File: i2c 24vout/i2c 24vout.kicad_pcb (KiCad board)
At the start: 2 copper layers, 131.2 x 55 mm, 79 parts, among them J1 power in, J2 Conn_01x04, J3 Conn_01x04, J4 Conn_01x04, J5 Conn_01x04, J6 to qwiic breakout, J8 Conn_01x01, J9 Conn_01x01, U1 ILQ620GB-X009, U2 ILQ620GB-X009, U3 ILQ620GB-X009, U4 ILQ620GB-X009, U5 PCA9685PW

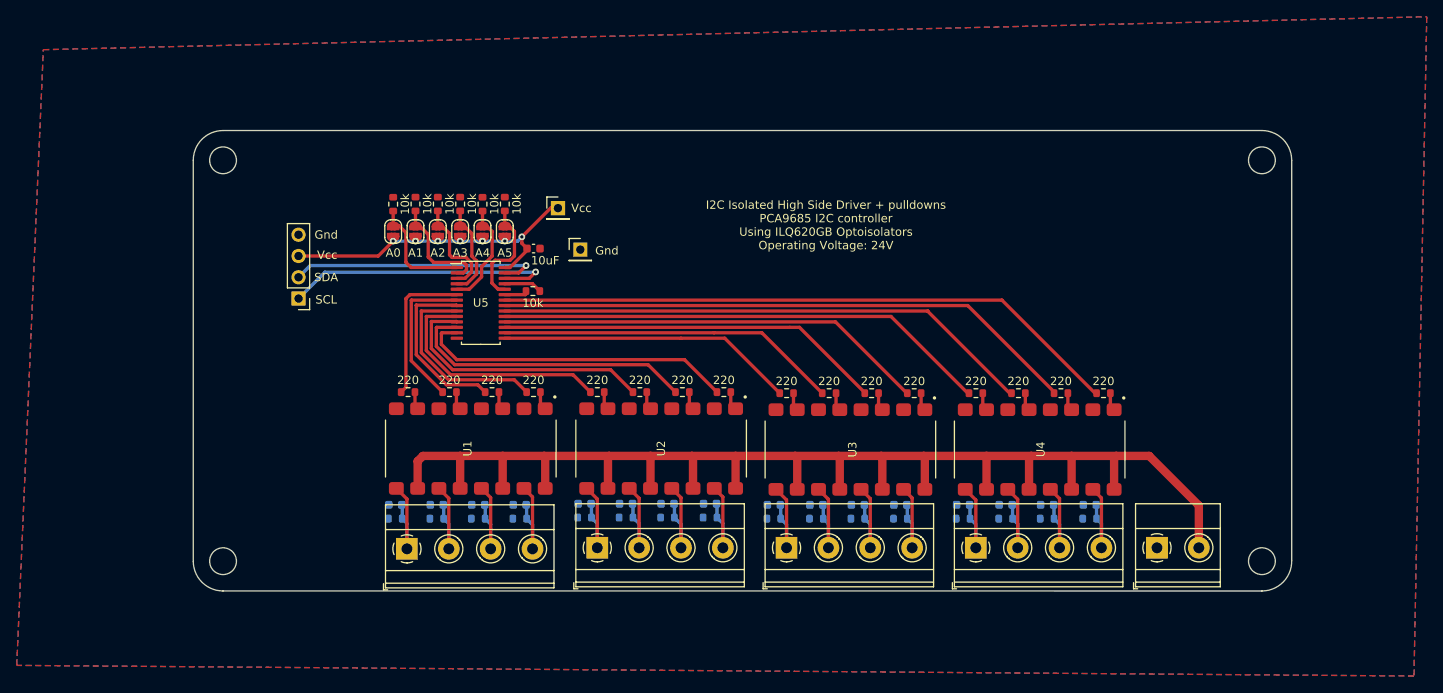
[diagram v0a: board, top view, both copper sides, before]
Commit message: shrank boards
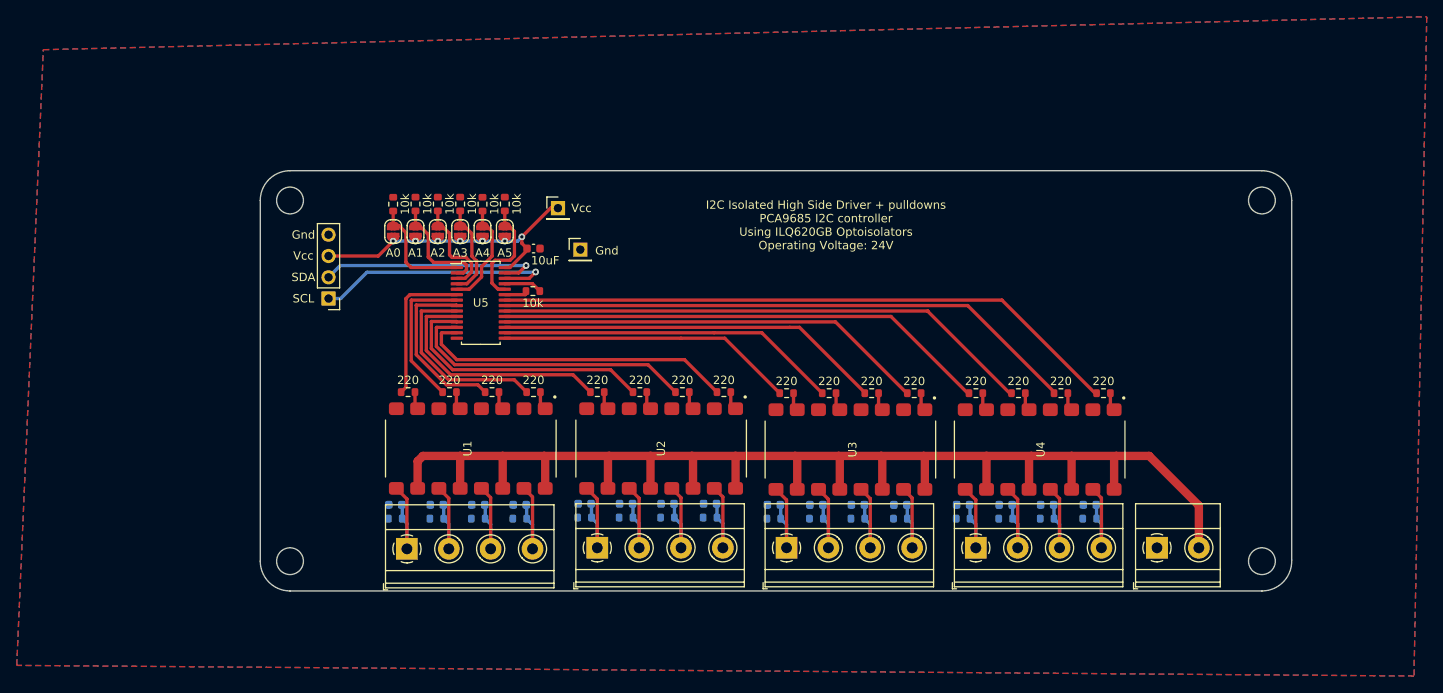
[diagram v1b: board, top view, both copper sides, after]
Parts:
- moved REF** 9.33 mm to (94.4, 83.8)
- moved REF** 8.00 mm to (94.4, 126.9)
- moved REF** 4.80 mm to (210.5, 83.8)
- moved J6 3.58 mm to (99.0, 95.5)
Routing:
- net /sda: track 30.7 -> 27.1 mm
- net VCC: track 38.7 -> 35.2 mm
- net /scl: track 33.6 -> 30.1 mm
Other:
- board size 131.2 x 55 mm -> 123.2 x 50.2 mm
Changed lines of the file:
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@@
   )
   (footprint "MountingHole:MountingHole_3.2mm_M3" (layer "F.Cu")
-    (at 86.4 79.034)
+    (at 94.4 83.834)
     (descr "Mounting Hole 3.2mm, no annular, M3")
     (tags "mounting hole 3.2mm no annular m3")
@@
   )
   (footprint "Connector_PinHeader_2.54mm:PinHeader_1x04_P2.54mm_Vertical" (layer "F.Cu")
-    (at 95.417 95.544 180)
+    (at 99 95.544 180)
     (descr "Through hole straight pin header, 1x04, 2.54mm pitch, single row")
     (tags "Through hole pin header THT 1x04 2.54mm single row")
@@
   )
   (footprint "MountingHole:MountingHole_3.2mm_M3" (layer "F.Cu")
-    (at 210.479 79.034)
+    (at 210.479 83.834)
     (descr "Mounting Hole 3.2mm, no annular, M3")
     (tags "mounting hole 3.2mm no annular m3")
@@
   )
   (footprint "MountingHole:MountingHole_3.2mm_M3" (layer "F.Cu")
-    (at 86.4 126.913)
+    (at 94.4 126.913)
     (descr "Mounting Hole 3.2mm, no annular, M3")
     (tags "mounting hole 3.2mm no annular m3")
@@
     )
   )
-  (gr_arc (start 86.4 130.469) (mid 83.885528 129.427472) (end 82.844 126.913) (layer "Edge.Cuts") (width 0.1))
-  (gr_line (start 82.844 79.034) (end 82.844 126.913) (layer "Edge.Cuts") (width 0.1))
-  (gr_line (start 86.4 75.478) (end 210.479 75.478) (layer "Edge.Cuts") (width 0.1))
-  (gr_line (start 210.479 130.471267) (end 86.4 130.469) (layer "Edge.Cuts") (width 0.1))
+  (gr_arc (start 94.4 130.469) (mid 91.885528 129.427472) (end 90.844 126.913) (layer "Edge.Cuts") (width 0.1))
+  (gr_line (start 90.844 83.834) (end 90.844 126.913) (layer "Edge.Cuts") (width 0.1))
+  (gr_line (start 94.4 80.278) (end 210.479 80.278) (layer "Edge.Cuts") (width 0.1))
+  (gr_line (start 210.479 130.471267) (end 94.4 130.469) (layer "Edge.Cuts") (width 0.1))
   (gr_arc (start 214.035 126.786) (mid 213.039582 129.383766) (end 210.479 130.471267) (layer "Edge.Cuts") (width 0.1))
-  (gr_arc (start 82.844 79.034) (mid 83.885528 76.519528) (end 86.4 75.478) (layer "Edge.Cuts") (width 0.1))
-  (gr_arc (start 210.479 75.478) (mid 212.993472 76.519528) (end 214.035 79.034) (layer "Edge.Cuts") (width 0.1))
-  (gr_line (start 214.035 79.034) (end 214.035 126.786) (layer "Edge.Cuts") (width 0.1))
+  (gr_arc (start 90.844 83.834) (mid 91.885528 81.319528) (end 94.4 80.278) (layer "Edge.Cuts") (width 0.1))
+  (gr_arc (start 210.479 80.278) (mid 212.993472 81.319528) (end 214.035 83.834) (layer "Edge.Cuts") (width 0.1))
+  (gr_line (start 214.035 83.834) (end 214.035 126.786) (layer "Edge.Cuts") (width 0.1))
   (gr_text "11" (at 168.696 128.691) (layer "B.SilkS")
     (effects (font (size 1 1) (thickness 0.15)) (justify mirror))
@@
     (effects (font (size 1 1) (thickness 0.15)) (justify mirror))
   )
-  (gr_text "Gnd" (at 98.846 87.924) (layer "B.SilkS")
+  (gr_text "Gnd" (at 96 88) (layer "B.SilkS")
     (effects (font (size 1 1) (thickness 0.15)) (justify mirror))
   )
-  (gr_text "SCL" (at 98.846 95.671) (layer "B.SilkS")
+  (gr_text "SCL" (at 96 95.671) (layer "B.SilkS")
     (effects (font (size 1 1) (thickness 0.15)) (justify mirror))
   )
@@
     (effects (font (size 1 1) (thickness 0.15)) (justify mirror))
   )
-  (gr_text "Vcc" (at 98.719 90.337) (layer "B.SilkS")
+  (gr_text "Vcc" (at 96 90.337) (layer "B.SilkS")
     (effects (font (size 1 1) (thickness 0.15)) (justify mirror))
   )
@@
     (effects (font (size 1 1) (thickness 0.15)) (justify mirror))
   )
-  (gr_text "SDA" (at 98.846 93.004) (layer "B.SilkS")
+  (gr_text "SDA" (at 96 93) (layer "B.SilkS")
     (effects (font (size 1 1) (thickness 0.15)) (justify mirror))
   )
@@
     (effects (font (size 1 1) (thickness 0.15)))
   )
-  (gr_text "SCL" (at 98.719 95.681) (layer "F.SilkS")
+  (gr_text "SCL" (at 96 95.544) (layer "F.SilkS")
     (effects (font (size 1 1) (thickness 0.15)))
   )
@@
     (effects (font (size 1 1) (thickness 0.15)))
   )
-  (gr_text "SDA" (at 98.719 93.014) (layer "F.SilkS")
+  (gr_text "SDA" (at 96 93) (layer "F.SilkS")
     (effects (font (size 1 1) (thickness 0.15)))
   )
-  (gr_text "Vcc" (at 98.846 90.347) (layer "F.SilkS")
+  (gr_text "Vcc" (at 96 90.434) (layer "F.SilkS")
     (effects (font (size 1 1) (thickness 0.15)))
   )
@@
     (effects (font (size 1 1) (thickness 0.15)))
   )
-  (gr_text "Gnd" (at 98.719 87.934) (layer "F.SilkS")
+  (gr_text "Gnd" (at 96 87.934) (layer "F.SilkS")
     (effects (font (size 1 1) (thickness 0.15)))
   )
@@
   (segment (start 120.67585 91.834) (end 122.709 89.80085) (width 0.4) (layer "F.Cu") (net 18))
   (segment (start 125.516 84.749) (end 126.405 84.749) (width 0.4) (layer "F.Cu") (net 18))
-  (segment (start 95.417 90.464) (end 104.942 90.464) (width 0.4) (layer "F.Cu") (net 18))
   (segment (start 122.087 88.178) (end 125.516 84.749) (width 0.4) (layer "F.Cu") (net 18))
   (segment (start 104.942 90.464) (end 106.72 88.686) (width 0.4) (layer "F.Cu") (net 18))
+  (segment (start 104.942 90.464) (end 99 90.464) (width 0.4) (layer "F.Cu") (net 18))
   (via (at 120.055 88.686) (size 0.8) (drill 0.4) (layers "F.Cu" "B.Cu") (net 18))
   (via (at 114.721 88.686) (size 0.8) (drill 0.4) (layers "F.Cu" "B.Cu") (net 18))
@@
   (segment (start 122.973 93.134) (end 123.738 92.369) (width 0.4) (layer "F.Cu") (net 20))
   (via (at 123.738 92.369) (size 0.8) (drill 0.4) (layers "F.Cu" "B.Cu") (net 20))
-  (segment (start 95.417 95.544) (end 98.554489 92.406511) (width 0.4) (layer "B.Cu") (net 20))
-  (segment (start 123.700489 92.406511) (end 123.738 92.369) (width 0.4) (layer "B.Cu") (net 20))
-  (segment (start 98.554489 92.406511) (end 123.700489 92.406511) (width 0.4) (layer "B.Cu") (net 20))
+  (segment (start 123.700489 92.406511) (end 103.593489 92.406511) (width 0.4) (layer "B.Cu") (net 20))
+  (segment (start 100.456 95.544) (end 99 95.544) (width 0.4) (layer "B.Cu") (net 20))
+  (segment (start 123.738 92.369) (end 123.700489 92.406511) (width 0.4) (layer "B.Cu") (net 20))
+  (segment (start 103.593489 92.406511) (end 100.456 95.544) (width 0.4) (layer "B.Cu") (net 20))
   (segment (start 120.0475 92.484) (end 121.718 92.484) (width 0.4) (layer "F.Cu") (net 21))
   (segment (start 121.718 92.484) (end 122.595 91.607) (width 0.4) (layer "F.Cu") (net 21))
   (via (at 122.595 91.607) (size 0.8) (drill 0.4) (layers "F.Cu" "B.Cu") (net 21))
-  (segment (start 96.814 91.607) (end 95.417 93.004) (width 0.4) (layer "B.Cu") (net 21))
-  (segment (start 122.595 91.607) (end 96.814 91.607) (width 0.4) (layer "B.Cu") (net 21))
+  (segment (start 100.397 91.607) (end 99 93.004) (width 0.4) (layer "B.Cu") (net 21))
+  (segment (start 122.595 91.607) (end 100.397 91.607) (width 0.4) (layer "B.Cu") (net 21))
   (segment (start 108.23748 87.66348) (end 107.467 86.893) (width 0.4) (layer "F.Cu") (net 22))
   (segment (start 107.467 86.893) (end 106.72 86.893) (width 0.4) (layer "F.Cu") (net 22))

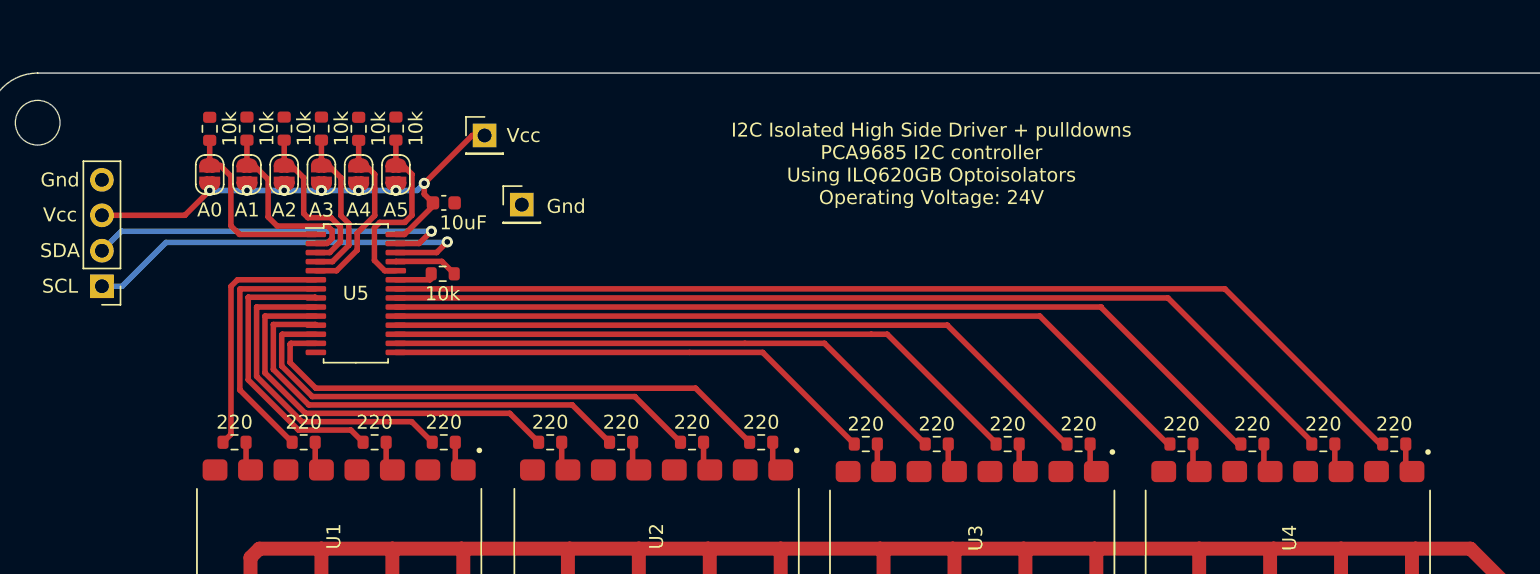
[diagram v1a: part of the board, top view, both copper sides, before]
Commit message: added qwiic connectors to boards as well as breakout connector
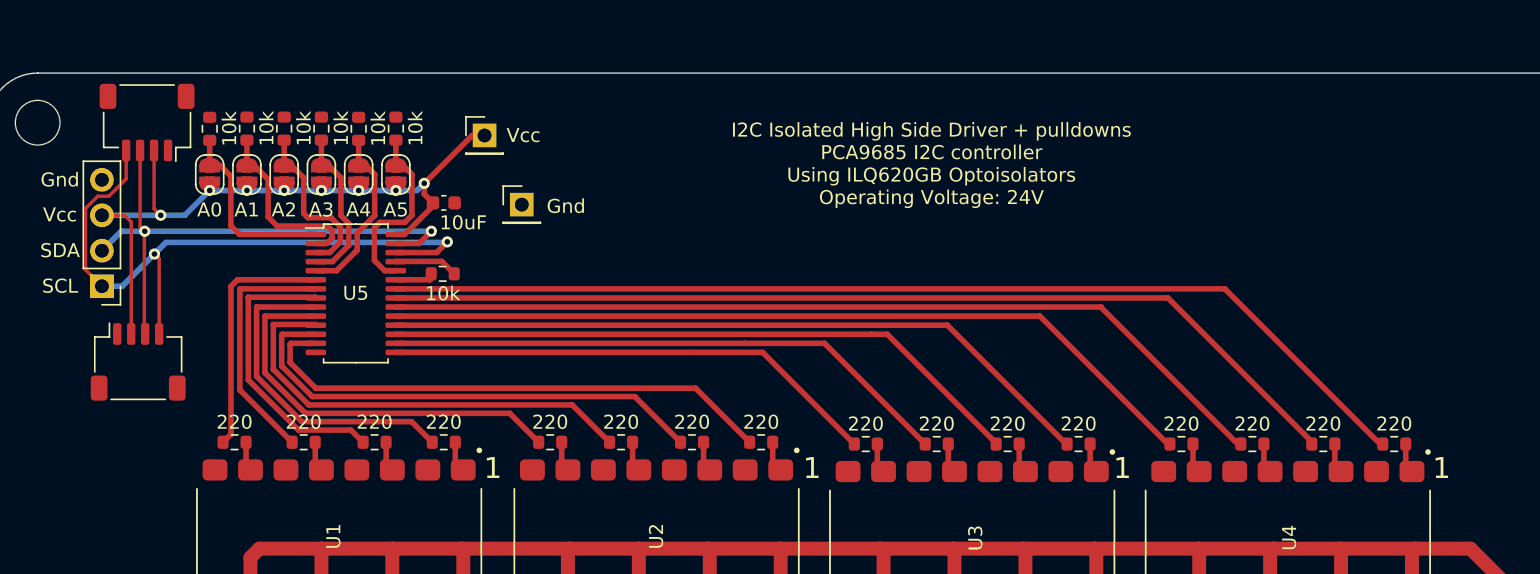
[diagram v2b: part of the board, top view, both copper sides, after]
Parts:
- added J7: qwiic 1, Connector_JST:JST_SH_SM04B-SRSS-TB_1x04-1MP_P1.00mm_Horizontal, F.Cu at (101.6, 101.0)
- added J8: qwiic 2, Connector_JST:JST_SH_SM04B-SRSS-TB_1x04-1MP_P1.00mm_Horizontal, F.Cu at (102.2, 83.8)
- J9: renamed from J8; value Conn_01x01 -> qwiic 2
- renumbered J9 to J10
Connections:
- J9 pad 1: VCC -> /scl
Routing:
- net /scl: track 30.1 -> 47.8 mm, vias 1 -> 2
- net VCC: track 35.2 -> 50.3 mm, vias 7 -> 8
- net /sda: track 27.1 -> 40.4 mm, vias 1 -> 2

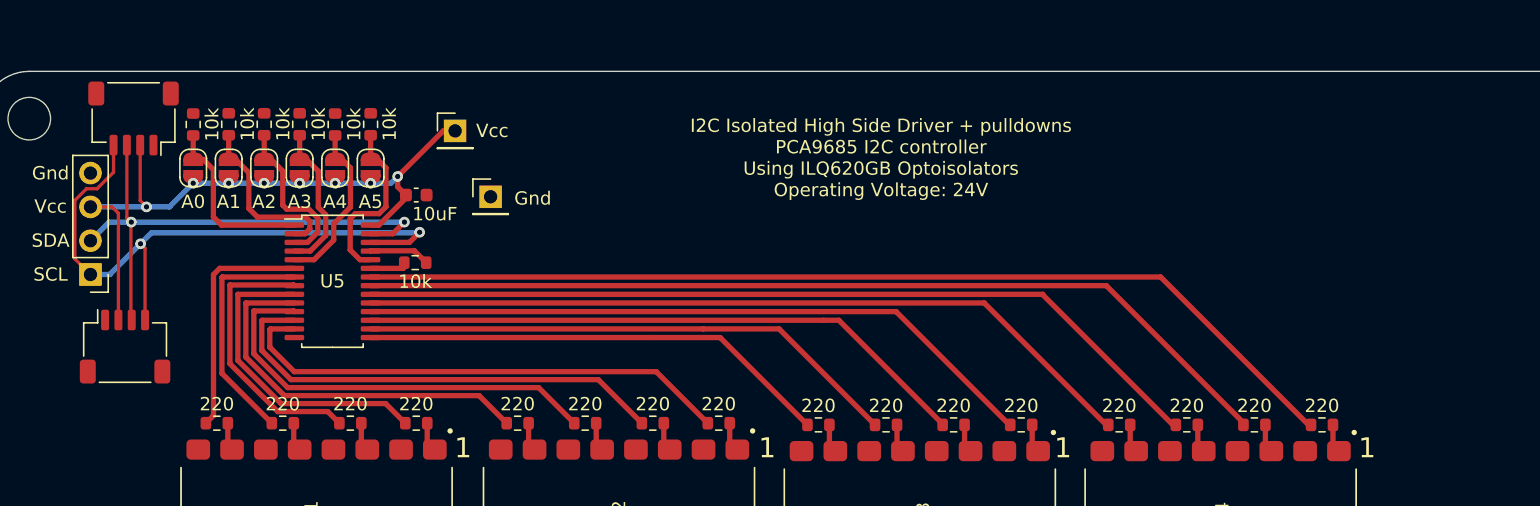
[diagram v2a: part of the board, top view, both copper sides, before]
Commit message: reel detent added
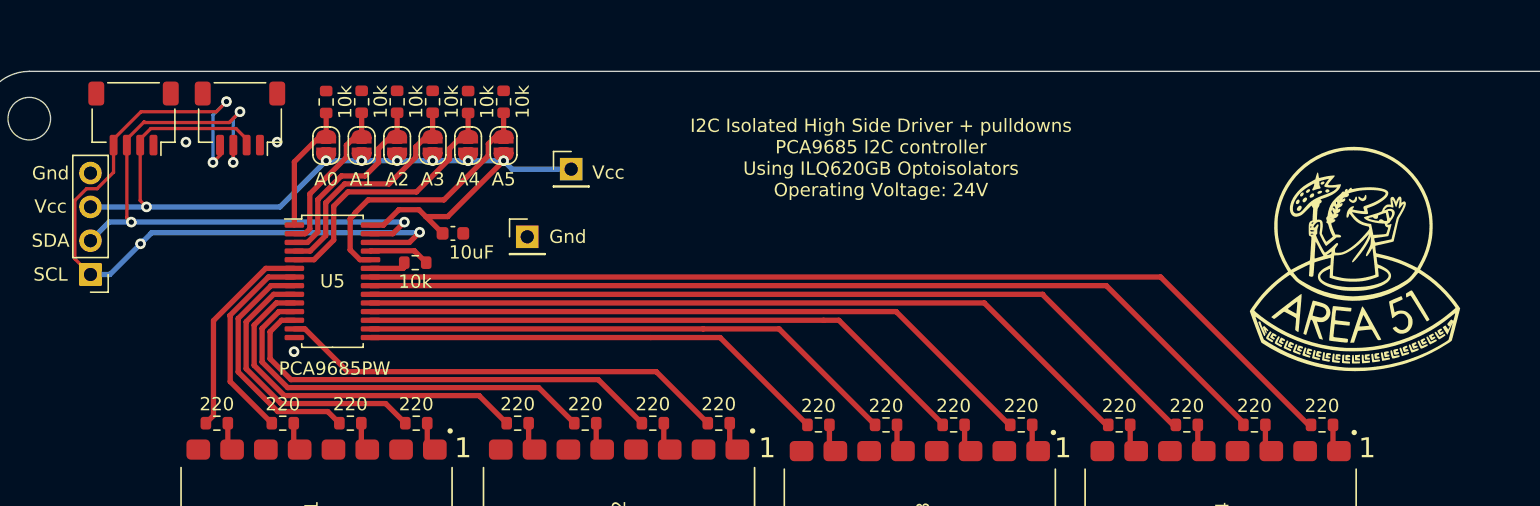
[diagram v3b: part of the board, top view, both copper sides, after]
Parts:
- added G***: LOGO, Evan's misc parts:LC API, F.Cu at (193.5, 94.5)
- J9: value qwiic 2 -> Conn_01x01
- moved J7 19.2 mm to (110.2, 83.8), turned to 180 degrees
- moved JP1 10.1 mm to (116.7, 85.9)
- moved JP2 10.1 mm to (119.4, 85.9)
- moved JP3 10.1 mm to (122.0, 85.9)
- moved JP4 10.1 mm to (124.7, 85.9)
- moved JP5 10.1 mm to (127.4, 85.9)
- moved JP6 10.1 mm to (130.0, 85.9)
- moved R33 10.1 mm to (116.7, 82.6)
- moved R34 10.1 mm to (119.4, 82.6)
- moved R35 10.1 mm to (122.0, 82.6)
- moved R36 10.1 mm to (124.7, 82.6)
- moved R37 10.1 mm to (127.4, 82.6)
- moved R38 10.1 mm to (130.0, 82.6)
- moved J9 9.19 mm to (135.1, 87.6)
- moved J10 4.08 mm to (131.8, 92.7)
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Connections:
- J9 pad 1: /scl -> VCC
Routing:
- net VCC: track 50.3 -> 66.4 mm, vias 8 -> 7
- net /scl: track 47.8 -> 58.6 mm, vias 2 -> 4
- net Net-(JP5-Pad2): track 12.7 -> 20.6 mm
- net /sda: track 40.4 -> 48.2 mm, vias 2 -> 4
- net Net-(JP6-Pad2): track 13.4 -> 20.6 mm
- net Net-(JP4-Pad2): track 11.5 -> 17.6 mm
- net /pwm7: track 38.5 -> 34.0 mm
- net Net-(JP1-Pad2): track 13.5 -> 9.72 mm
- net Net-(JP3-Pad2): track 12.3 -> 14.9 mm
- net /pwm1: track 18.0 -> 15.4 mm
- net /pwm2: track 20.9 -> 18.5 mm
- net /pwm3: track 23.7 -> 21.7 mm
- net /pwm0: track 17.7 -> 15.6 mm
- net /pwm4: track 29.4 -> 27.5 mm
- net /pwm5: track 32.5 -> 30.8 mm
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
